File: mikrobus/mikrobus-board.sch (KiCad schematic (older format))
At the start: 7 parts, among them J1 Conn_01x04, P3 microBus_1, P4 microBus_2, P5 microBus_1, P6 microBus_2

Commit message: update connector
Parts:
- removed J1: Conn_01x04, Pin_Headers:Pin_Header_Straight_1x04_Pitch2.54mm, symbol Conn_01x04
- added J1: Conn_01x06, Pin_Headers:Pin_Header_Straight_1x06_Pitch2.54mm, symbol Conn_01x06
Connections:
- wire segments 72 -> 74
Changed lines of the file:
@@
 $EndComp
 $Comp
-L +3.3V #PWR01
+L +3.3V #PWR9
 U 1 1 5A7F089C
 P 8200 6300
-F 0 "#PWR01" H 8200 6150 50  0001 C CNN
+F 0 "#PWR9" H 8200 6150 50  0001 C CNN
 F 1 "+3.3V" H 8200 6440 50  0000 C CNN
 F 2 "" H 8200 6300 50  0001 C CNN
@@
 TX_1
 $Comp
-L GND #PWR02
+L GND #PWR3
 U 1 1 5732FDAE
 P 4750 8000
-F 0 "#PWR02" H 4750 7750 50  0001 C CNN
+F 0 "#PWR3" H 4750 7750 50  0001 C CNN
 F 1 "GND" H 4750 7850 50  0000 C CNN
 F 2 "" H 4750 8000 50  0000 C CNN
@@
 RST_1
 $Comp
-L +3.3V #PWR03
+L +3.3V #PWR1
 U 1 1 5ABB8932
 P 3350 7800
-F 0 "#PWR03" H 3350 7650 50  0001 C CNN
+F 0 "#PWR1" H 3350 7650 50  0001 C CNN
 F 1 "+3.3V" H 3350 7940 50  0000 C CNN
 F 2 "" H 3350 7800 50  0001 C CNN
@@
 TX_2
 $Comp
-L GND #PWR04
+L GND #PWR6
 U 1 1 5ABB8B45
 P 6100 8000
-F 0 "#PWR04" H 6100 7750 50  0001 C CNN
+F 0 "#PWR6" H 6100 7750 50  0001 C CNN
 F 1 "GND" H 6100 7850 50  0000 C CNN
 F 2 "" H 6100 8000 50  0000 C CNN
@@
 $EndComp
 $Comp
-L GND #PWR05
+L GND #PWR7
 U 1 1 5ABB8B4B
 P 7200 8000
-F 0 "#PWR05" H 7200 7750 50  0001 C CNN
+F 0 "#PWR7" H 7200 7750 50  0001 C CNN
 F 1 "GND" H 7200 7850 50  0000 C CNN
 F 2 "" H 7200 8000 50  0000 C CNN
@@
 RST_2
 NoConn ~ 7550 5300
-$Comp
-L Conn_01x04 J1
-U 1 1 5ABB9346
-P 9650 7250
-F 0 "J1" H 9650 7450 50  0000 C CNN
-F 1 "Conn_01x04" H 9650 6950 50  0000 C CNN
-F 2 "Pin_Headers:Pin_Header_Straight_1x04_Pitch2.54mm" H 9650 7250 50  0001 C CNN
-F 3 "" H 9650 7250 50  0001 C CNN
-	1    9650 7250
-	1    0    0    -1
-$EndComp
 Text Label 8950 7150 0    60   ~ 0
 EXT_1
@@
 EXT_4
 $Comp
-L GND #PWR06
+L GND #PWR5
 U 1 1 5ABB9FEC
 P 5950 6450
-F 0 "#PWR06" H 5950 6200 50  0001 C CNN
+F 0 "#PWR5" H 5950 6200 50  0001 C CNN
 F 1 "GND" H 5950 6300 50  0000 C CNN
 F 2 "" H 5950 6450 50  0001 C CNN
@@
 $EndComp
 $Comp
-L +3.3V #PWR07
+L +3.3V #PWR4
 U 1 1 5ABBA05D
 P 5850 7800
-F 0 "#PWR07" H 5850 7650 50  0001 C CNN
+F 0 "#PWR4" H 5850 7650 50  0001 C CNN
 F 1 "+3.3V" H 5850 7940 50  0000 C CNN
 F 2 "" H 5850 7800 50  0001 C CNN
@@
 	5850 7800 6200 7800
 $Comp
-L GND #PWR08
+L GND #PWR2
 U 1 1 5ABBA17A
 P 3650 7900
-F 0 "#PWR08" H 3650 7650 50  0001 C CNN
+F 0 "#PWR2" H 3650 7650 50  0001 C CNN
 F 1 "GND" H 3650 7750 50  0000 C CNN
 F 2 "" H 3650 7900 50  0001 C CNN
@@
 $EndComp
 $Comp
-L GND #PWR09
+L GND #PWR8
 U 1 1 5ABBA41C
 P 8150 6100
-F 0 "#PWR09" H 8150 5850 50  0001 C CNN
+F 0 "#PWR8" H 8150 5850 50  0001 C CNN
 F 1 "GND" H 8150 5950 50  0000 C CNN
 F 2 "" H 8150 6100 50  0001 C CNN
@@
 Wire Wire Line
 	7550 6100 8150 6100
+$Comp
+L Conn_01x06 J1
+U 1 1 5ABB93C6
+P 9650 7350
+F 0 "J1" H 9650 7650 50  0000 C CNN
+F 1 "Conn_01x06" H 9650 6950 50  0000 C CNN
+F 2 "Pin_Headers:Pin_Header_Straight_1x06_Pitch2.54mm" H 9650 7350 50  0001 C CNN
+F 3 "" H 9650 7350 50  0001 C CNN
+	1    9650 7350
+	1    0    0    -1
+$EndComp
+$Comp
+L +3.3V #PWR10
+U 1 1 5ABB93FE
+P 9150 7550
+F 0 "#PWR10" H 9150 7400 50  0001 C CNN
+F 1 "+3.3V" H 9150 7690 50  0000 C CNN
+F 2 "" H 9150 7550 50  0001 C CNN
+F 3 "" H 9150 7550 50  0001 C CNN
+	1    9150 7550
+	0    -1   -1   0
+$EndComp
+$Comp
+L GND #PWR11
+U 1 1 5ABB9420
+P 9150 7650
+F 0 "#PWR11" H 9150 7400 50  0001 C CNN
+F 1 "GND" H 9150 7500 50  0000 C CNN
+F 2 "" H 9150 7650 50  0001 C CNN
+F 3 "" H 9150 7650 50  0001 C CNN
+	1    9150 7650
+	0    1    1    0
+$EndComp
+Wire Wire Line
+	9150 7650 9450 7650
+Wire Wire Line
+	9150 7550 9450 7550
 $EndSCHEMATC

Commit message: Finished routing
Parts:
- P3, P4, P5, P6: footprint Pin_Headers:Pin_Header_Straight_1x08_Pitch2.54mm -> Socket_Strips:Socket_Strip_Straight_1x08_Pitch2.54mm
- UPDUINO2_DOWN1: footprint Pin_Headers:Pin_Header_Straight_1x16_Pitch2.54mm -> Socket_Strips:Socket_Strip_Straight_1x16_Pitch2.54mm
- UPDUINO2_UP1: footprint Pin_Headers:Pin_Header_Straight_1x18_Pitch2.54mm -> Socket_Strips:Socket_Strip_Straight_1x18_Pitch2.54mm
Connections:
- net EXT_1: now also J1.4 (Pin_4); no longer J1.1 (Pin_1)
- net EXT_2: now also J1.3 (Pin_3); no longer J1.2 (Pin_2)
- net EXT_3: now also J1.2 (Pin_2); no longer J1.3 (Pin_3)
- net EXT_4: now also J1.1 (Pin_1); no longer J1.4 (Pin_4)
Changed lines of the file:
@@
 EESchema Schematic File Version 2
-LIBS:mikrobus-board-rescue
 LIBS:power
 LIBS:device
@@
 F 0 "UPDUINO2_UP1" H 6700 6400 50  0000 C CNN
 F 1 "Conn_01x18" H 6700 4500 50  0000 C CNN
-F 2 "Pin_Headers:Pin_Header_Straight_1x18_Pitch2.54mm" H 6700 5500 50  0001 C CNN
+F 2 "Socket_Strips:Socket_Strip_Straight_1x18_Pitch2.54mm" H 6700 5500 50  0001 C CNN
 F 3 "" H 6700 5500 50  0001 C CNN
 	1    6700 5500
@@
 F 0 "UPDUINO2_DOWN1" H 7350 6200 50  0000 C CNN
 F 1 "Conn_01x16" H 7350 4500 50  0000 C CNN
-F 2 "Pin_Headers:Pin_Header_Straight_1x16_Pitch2.54mm" H 7350 5400 50  0001 C CNN
+F 2 "Socket_Strips:Socket_Strip_Straight_1x16_Pitch2.54mm" H 7350 5400 50  0001 C CNN
 F 3 "" H 7350 5400 50  0001 C CNN
 	1    7350 5400
@@
 F 0 "P3" H 3950 7950 50  0000 C CNN
 F 1 "microBus_1" V 4050 7500 50  0000 C CNN
-F 2 "Pin_Headers:Pin_Header_Straight_1x08_Pitch2.54mm" H 3950 7500 50  0001 C CNN
+F 2 "Socket_Strips:Socket_Strip_Straight_1x08_Pitch2.54mm" H 3950 7500 50  0001 C CNN
 F 3 "" H 3950 7500 50  0000 C CNN
 	1    3950 7500
@@
 F 0 "P4" H 5050 7950 50  0000 C CNN
 F 1 "microBus_2" V 5150 7500 50  0000 C CNN
-F 2 "Pin_Headers:Pin_Header_Straight_1x08_Pitch2.54mm" H 5050 7500 50  0001 C CNN
+F 2 "Socket_Strips:Socket_Strip_Straight_1x08_Pitch2.54mm" H 5050 7500 50  0001 C CNN
 F 3 "" H 5050 7500 50  0000 C CNN
 	1    5050 7500
@@
 F 0 "P5" H 6400 7950 50  0000 C CNN
 F 1 "microBus_1" V 6500 7500 50  0000 C CNN
-F 2 "Pin_Headers:Pin_Header_Straight_1x08_Pitch2.54mm" H 6400 7500 50  0001 C CNN
+F 2 "Socket_Strips:Socket_Strip_Straight_1x08_Pitch2.54mm" H 6400 7500 50  0001 C CNN
 F 3 "" H 6400 7500 50  0000 C CNN
 	1    6400 7500
@@
 F 0 "P6" H 7500 7950 50  0000 C CNN
 F 1 "microBus_2" V 7600 7500 50  0000 C CNN
-F 2 "Pin_Headers:Pin_Header_Straight_1x08_Pitch2.54mm" H 7500 7500 50  0001 C CNN
+F 2 "Socket_Strips:Socket_Strip_Straight_1x08_Pitch2.54mm" H 7500 7500 50  0001 C CNN
 F 3 "" H 7500 7500 50  0000 C CNN
 	1    7500 7500
@@
 NoConn ~ 7550 5300
 Text Label 8950 7150 0    60   ~ 0
+EXT_4
+Text Label 8950 7250 0    60   ~ 0
+EXT_3
+Text Label 8950 7350 0    60   ~ 0
+EXT_2
+Text Label 8950 7450 0    60   ~ 0
 EXT_1
-Text Label 8950 7250 0    60   ~ 0
-EXT_2
-Text Label 8950 7350 0    60   ~ 0
-EXT_3
-Text Label 8950 7450 0    60   ~ 0
-EXT_4
 $Comp
 L GND #PWR5

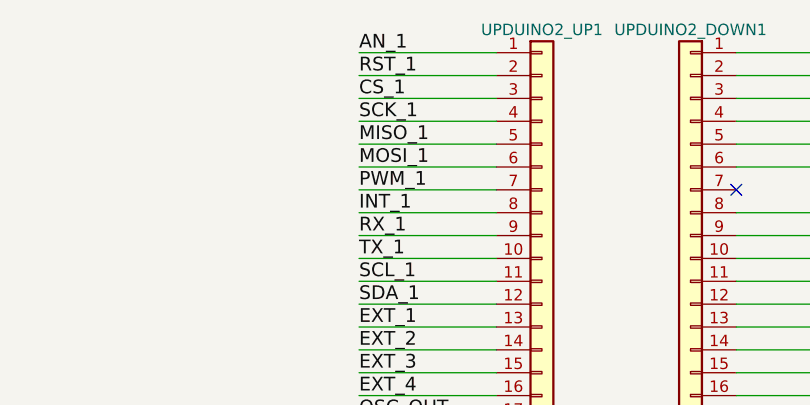
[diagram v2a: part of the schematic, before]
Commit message: Simpler routing
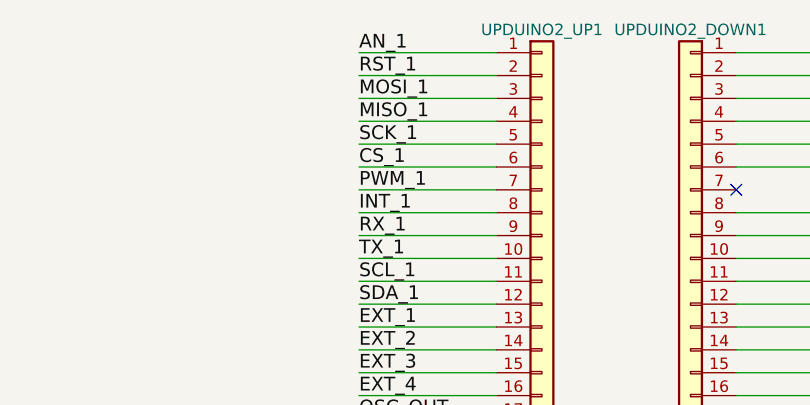
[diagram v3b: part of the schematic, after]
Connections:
- net CS_1: now also UPDUINO2_UP1.6 (Pin_6); no longer UPDUINO2_UP1.3 (Pin_3)
- net MISO_1: now also UPDUINO2_UP1.4 (Pin_4); no longer UPDUINO2_UP1.5 (Pin_5)
- net MOSI_1: now also UPDUINO2_UP1.3 (Pin_3); no longer UPDUINO2_UP1.6 (Pin_6)
- net SCK_1: now also UPDUINO2_UP1.5 (Pin_5); no longer UPDUINO2_UP1.4 (Pin_4)
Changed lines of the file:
@@
 RST_1
 Text Label 5900 4900 0    60   ~ 0
+MOSI_1
+Text Label 5900 5000 0    60   ~ 0
+MISO_1
+Text Label 5900 5100 0    60   ~ 0
+SCK_1
+Text Label 5900 5200 0    60   ~ 0
 CS_1
-Text Label 5900 5000 0    60   ~ 0
-SCK_1
-Text Label 5900 5100 0    60   ~ 0
-MISO_1
-Text Label 5900 5200 0    60   ~ 0
-MOSI_1
 Text Label 5900 5300 0    60   ~ 0
 PWM_1
